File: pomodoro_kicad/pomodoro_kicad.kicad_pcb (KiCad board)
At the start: 2 copper layers, 48 parts, among them J1 LiPO PH2.0, J10 LED_VCC, J11 LED_DATA, J12 LED_GND, J2 Conn_01x04, J3 VDD, J4 GND, J5 SCK, J6 WS, J7 SD, J8 L/R, J9 USB_C_Receptacle_USB2.0_16P, Q1 IRLML6402, SW1 RotaryEncoder_Switch, U1 AP2112K-3.3, U2 MCP73831-2-OT, U3 ESP32-S3-WROOM-1-N16R8

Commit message: Assign footprints with actual parts
assigned:
- capacitors
- LEDs
- diode
- resistors
- push button
- usb receptacle
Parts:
- moved C5 10.00 mm to (130.7, 137.5), turned to 0 degrees
- moved R4 3.89 mm to (131.5, 141.3), turned to -90 degrees
- moved C2 3.61 mm to (133.6, 124.1)
- moved C6 3.61 mm to (146.5, 124.3)
- moved R2 3.61 mm to (136.5, 123.3)
- moved R3 3.61 mm to (137.0, 119.8)
- moved R5 3.61 mm to (142.5, 119.8)
- moved R6 3.61 mm to (143.2, 123.3)
- moved SW1 3.61 mm to (139.8, 135.1)
- moved C3 0.50 mm to (108.7, 102.0)
- moved C4 0.50 mm to (108.7, 104.5)
- moved R1 0.50 mm to (108.6, 107.0)
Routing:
- net /ROT_SW: track 33.0 -> 22.9 mm
- net /ROT_B: track 14.4 -> 8.13 mm
- net /ROT_A: track 23.5 -> 17.4 mm
- net /EN: track 39.6 -> 38.8 mm
- net Net-(R4-Pad2): track 6.01 -> 6.55 mm

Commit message: First PCB layout not correct positions
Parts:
- removed C13: 220uF, Capacitor_SMD:C_0603_1608Metric
- removed J2: Conn_01x04, Connector_PinSocket_2.54mm:PinSocket_1x04_P2.54mm_Vertical
- added C14: 220uF, Capacitor_SMD:CP_Elec_6.3x7.7, F.Cu at (116.0, 128.2)
- added J13: OLED_3V3, TestPoint:TestPoint_THTPad_D2.0mm_Drill1.0mm, F.Cu at (113.0, 138.0)
- added J14: OLED_GND, TestPoint:TestPoint_THTPad_D2.0mm_Drill1.0mm, F.Cu at (117.1, 138.0)
- added J15: OLED_SCK, TestPoint:TestPoint_THTPad_D2.0mm_Drill1.0mm, F.Cu at (121.1, 138.0)
- added J16: OLED_WS, TestPoint:TestPoint_THTPad_D2.0mm_Drill1.0mm, F.Cu at (125.2, 138.0)
- C1, C10, C11, C12, C2, C3, C4, C6, C7, C8, C9: footprint Capacitor_SMD:C_0603_1608Metric -> Capacitor_SMD:C_0402_1005Metric
- C5: value 100nF -> 0.1uF; footprint Capacitor_SMD:C_0603_1608Metric -> Capacitor_SMD:C_0402_1005Metric
- D3: footprint Diode_SMD:D_SMA -> Diode_SMD:D_SOD-123F
- J1: footprint Connector_JST:JST_PH_B2B-PH-K_1x02_P2.00mm_Vertical -> Connector_JST:JST_PH_S2B-PH-SM4-TB_1x02-1MP_P2.00mm_Horizontal
- J9: footprint Connector_USB:USB_C_Receptacle_HRO_TYPE-C-31-M-12 -> _Footprints:SAMESKY_UJ20-C-H-G-SMT-1-P16-TR
- Q1: footprint Package_TO_SOT_SMD:SOT-23 -> Package_TO_SOT_SMD:SOT-23-3
- SW1: footprint customFootprints:rotaryEncoder -> _Footprints:rotaryEncoder
- SW2, SW3: footprint Button_Switch_SMD:SW_SPST_PTS645Sx43SMTR92 -> Button_Switch_SMD:SW_Tactile_SPST_NO_Straight_CK_PTS636Sx25SMTRLFS
- moved C8 7.80 mm to (105.0, 110.5), turned to -90 degrees
- moved J9 3.34 mm to (97.5, 80.2)
- moved SW2 2.25 mm to (100.5, 108.5)
- moved SW3 2.25 mm to (145.0, 107.0)
- moved J1 0.65 mm to (80.5, 101.8)
- moved R1 0.50 mm to (108.6, 106.5)
- moved R8 0.50 mm to (83.2, 108.0)
- moved C10 0.22 mm to (108.5, 99.5)
- moved U1 0.20 mm to (99.6, 98.0)
- moved C3 0.17 mm to (108.5, 102.0)
- moved C4 0.17 mm to (108.5, 104.5)
- moved C7 0.10 mm to (93.2, 98.0)
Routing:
- net /VBAT: track 31.9 -> 21.8 mm
- net /EN: track 38.8 -> 30.4 mm
- net GND: track 5.84 -> 0.00 mm
- net /OLED_SCL: track 21.0 -> 26.0 mm
- net /OLED_SDA: track 20.4 -> 24.9 mm
- net /ROT_SW: track 22.9 -> 26.0 mm
- net /ROT_B: track 8.13 -> 11.1 mm
- net /ROT_A: track 17.4 -> 20.3 mm
- net /VSYS: track 31.4 -> 28.7 mm
- net Net-(D1-K): track 2.50 -> 1.50 mm
- net /VBUS: track 44.6 -> 43.7 mm
- net /3V3: track 37.5 -> 36.9 mm

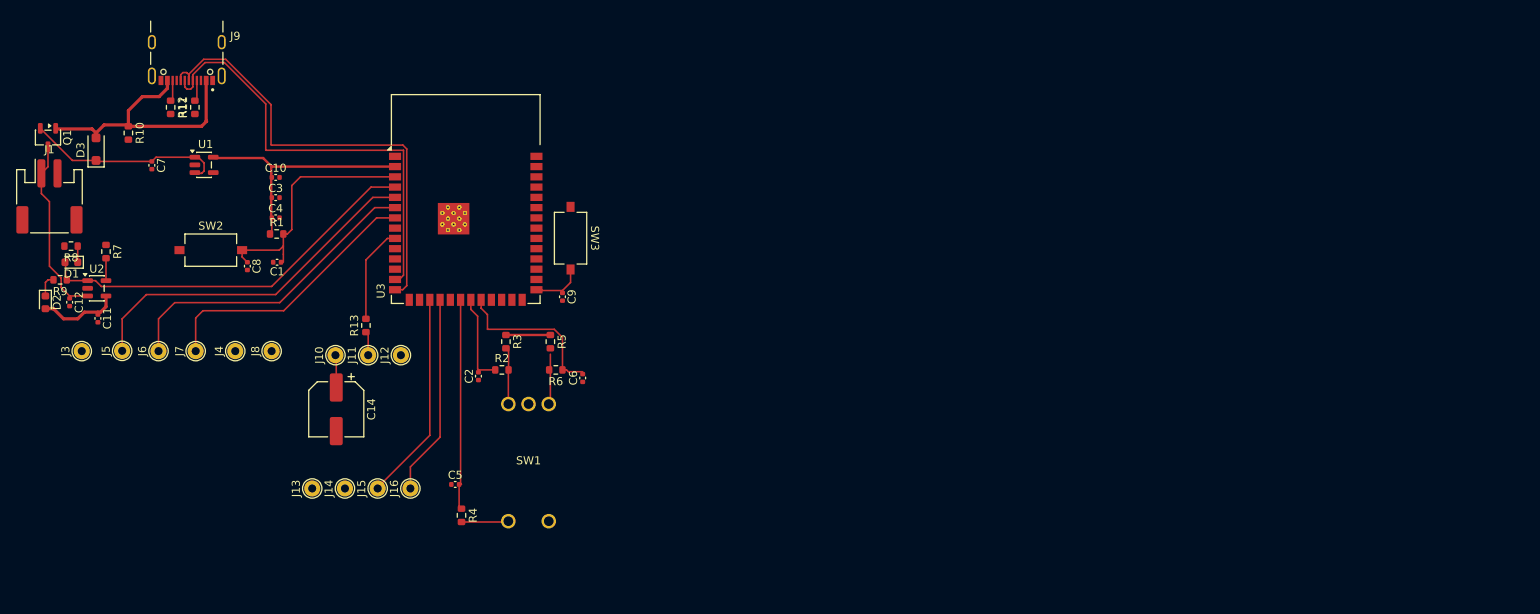
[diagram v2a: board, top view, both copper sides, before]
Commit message: Route PCB and update schematic pins for better connections
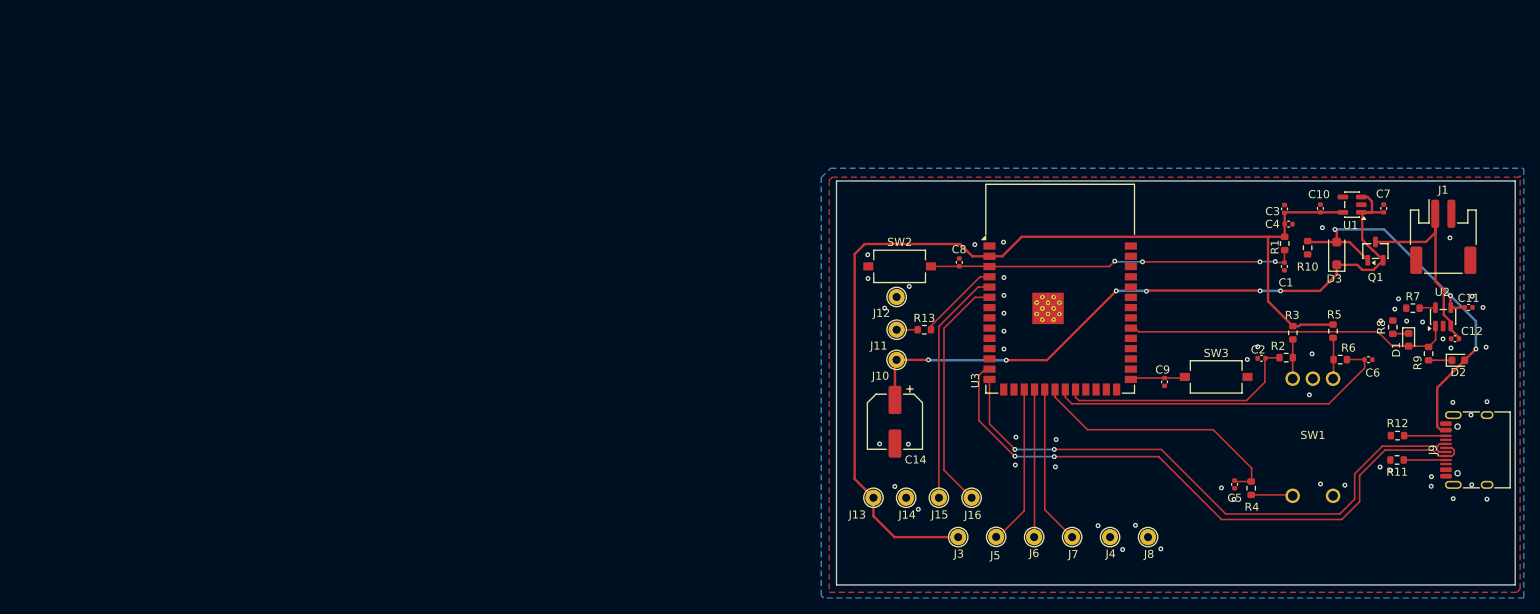
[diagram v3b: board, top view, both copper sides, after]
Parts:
- J9: footprint _Footprints:SAMESKY_UJ20-C-H-G-SMT-1-P16-TR -> Connector_USB:USB_C_Receptacle_HRO_TYPE-C-31-M-12
- moved D2 175.0 mm to (254.9, 122.1), turned to 0 degrees
- moved J1 172.6 mm to (253.0, 106.8)
- moved C12 171.5 mm to (254.5, 119.5), turned to 180 degrees
- moved C11 169.7 mm to (256.1, 115.6), turned to 0 degrees
- moved R9 169.6 mm to (251.2, 121.3), turned to -90 degrees
- moved J9 168.5 mm to (257.4, 133.2), turned to 90 degrees
- moved U2 166.7 mm to (253.0, 116.8), turned to 90 degrees
- moved D1 165.8 mm to (248.7, 119.6), turned to -90 degrees
- moved Q1 164.9 mm to (244.6, 108.6), turned to 90 degrees
- moved R8 163.9 mm to (246.8, 118.0), turned to 90 degrees
- moved R7 161.9 mm to (249.3, 115.7), turned to 0 degrees
- moved R12 157.2 mm to (247.4, 131.5), turned to 180 degrees
- moved R11 155.1 mm to (247.3, 134.5), turned to 0 degrees
- moved D3 154.1 mm to (239.8, 108.9)
- moved C7 152.6 mm to (245.7, 103.3), turned to 90 degrees
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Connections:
- U3 pad 17: /OLED_SCL -> /MIC_SCK
- U3 pad 18: /OLED_SDA -> /MIC_WS
- U3 pad 19: unconnected-(U3-IO11-Pad19) -> /MIC_SD
- U3 pad 21: /ROT_B -> /ROT_A
- U3 pad 22: /ROT_A -> /ROT_B
- U3 pad 32: unconnected-(U3-IO39-Pad32) -> /MCP_STAT
- U3 pad 4: /MCP_STAT -> /LED_DATA
- U3 pad 5: /MIC_SCK -> /OLED_SCL
- U3 pad 6: /MIC_WS -> /OLED_SDA
- U3 pad 7: /MIC_SD -> unconnected-(U3-IO7-Pad7)
- U3 pad 9: /LED_DATA -> unconnected-(U3-IO16-Pad9)
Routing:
- net /3V3: track 36.9 -> 128.1 mm
- net /VSYS: track 28.7 -> 85.8 mm, vias 0 -> 6
- net /MIC_SCK: track 44.0 -> 19.6 mm
- net /USB_D-: track 54.8 -> 78.6 mm, vias 0 -> 2
- net /ROT_A: track 20.3 -> 43.4 mm
- net /MIC_WS: track 39.0 -> 18.3 mm
- net /ROT_B: track 11.1 -> 30.3 mm
- net /USB_D+: track 57.4 -> 73.7 mm, vias 0 -> 2
- net /EN: track 30.4 -> 45.7 mm, vias 0 -> 4
- net /MIC_SD: track 33.9 -> 19.7 mm
- net /VBUS: track 43.7 -> 52.1 mm, vias 0 -> 3
- net /MCP_STAT: track 48.1 -> 40.8 mm
- net /ROT_SW: track 26.0 -> 32.7 mm
- net /VBAT: track 21.8 -> 26.8 mm
- net /OLED_SDA: track 24.9 -> 29.6 mm
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- added copper zone on B.Cu, net GND
- added copper zone on F.Cu, net GND
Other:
- board outline added: 84 x 50 mm

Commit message: Add stitching vias with 5mm spacing
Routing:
- net /VBUS: track 52.1 -> 58.8 mm
- net GND: track 0.00 -> 1.45 mm, vias 53 -> 136
